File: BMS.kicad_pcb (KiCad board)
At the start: 2 copper layers, 20 x 100 mm, 74 parts, among them Q2 PSMN3R7-100BSE, Q3 PSMN020-100YS, U1 MP2790DFP-0000-T

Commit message: bms layout progress
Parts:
- C_3V1, C_PACK_FLT1, C_REG1, C_REGIN1, C_TOP_FLT1, C_VDD1, D7, U1: moved to B.Cu
- D1, D2, D3, D4, D5, D6, D_CHG_VGS1, D_CHG_VGS2, MBAL_1, MBAL_2, MBAL_3, MBAL_4, MBAL_5, MBAL_6, R_BAL_5, R_BAL_6, R_CHG_PUP1, R_DSG_PUP1, R_GATE6: moved to F.Cu
- moved C_CELL_FLT6 82.0 mm to (210.1, 118.6), turned to 180 degrees
- moved MBAL_6 81.1 mm to (210.1, 113.2), turned to 90 degrees
- moved D_CHG_VGS2 81.0 mm to (208.8, 41.0), turned to -90 degrees
- moved R_CELL_FLT4 78.5 mm to (210.1, 117.0), turned to 180 degrees
- moved C_SRP_GND1 77.5 mm to (117.2, 101.9), turned to 90 degrees
- moved Q2 77.0 mm to (209.8, 53.6), turned to -90 degrees
- moved C_PACK_E1 76.6 mm to (106.0, 96.4)
- moved C_CELL_FLT5 74.8 mm to (210.1, 107.3), turned to 180 degrees
- moved C_SRN_GND1 74.7 mm to (114.7, 101.9), turned to 90 degrees
- moved C_SRN_SRP1 73.4 mm to (119.6, 101.9), turned to -90 degrees
- moved MBAL_5 71.2 mm to (209.9, 105.0), turned to 90 degrees
- moved C_CELL_FLT4 70.3 mm to (209.9, 99.3)
- moved D_CHG_VGS1 66.8 mm to (212.5, 63.4), turned to 90 degrees
- moved C_CELL_FLT3 66.2 mm to (209.9, 91.3), turned to 180 degrees
- moved D7 65.5 mm to (107.3, 85.3), turned to -90 degrees
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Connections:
- Q2 pad 3: /main/BMS/TOP -> /main/BMS/BATT+
- Q3 pad 3: /main/BMS/BATT+ -> /main/BMS/TOP
- R_CHG_MG1 pad 2: Net-(Q2-G) -> Net-(Q3-G)
- R_DSG_MG1 pad 2: Net-(Q3-G) -> Net-(Q2-G)
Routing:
- net /main/BMS/TOP: track 0.00 -> 1.62 mm
- added copper zone on B.Cu, net Net-(U1-VMID)
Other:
- copper layers 2 -> 4

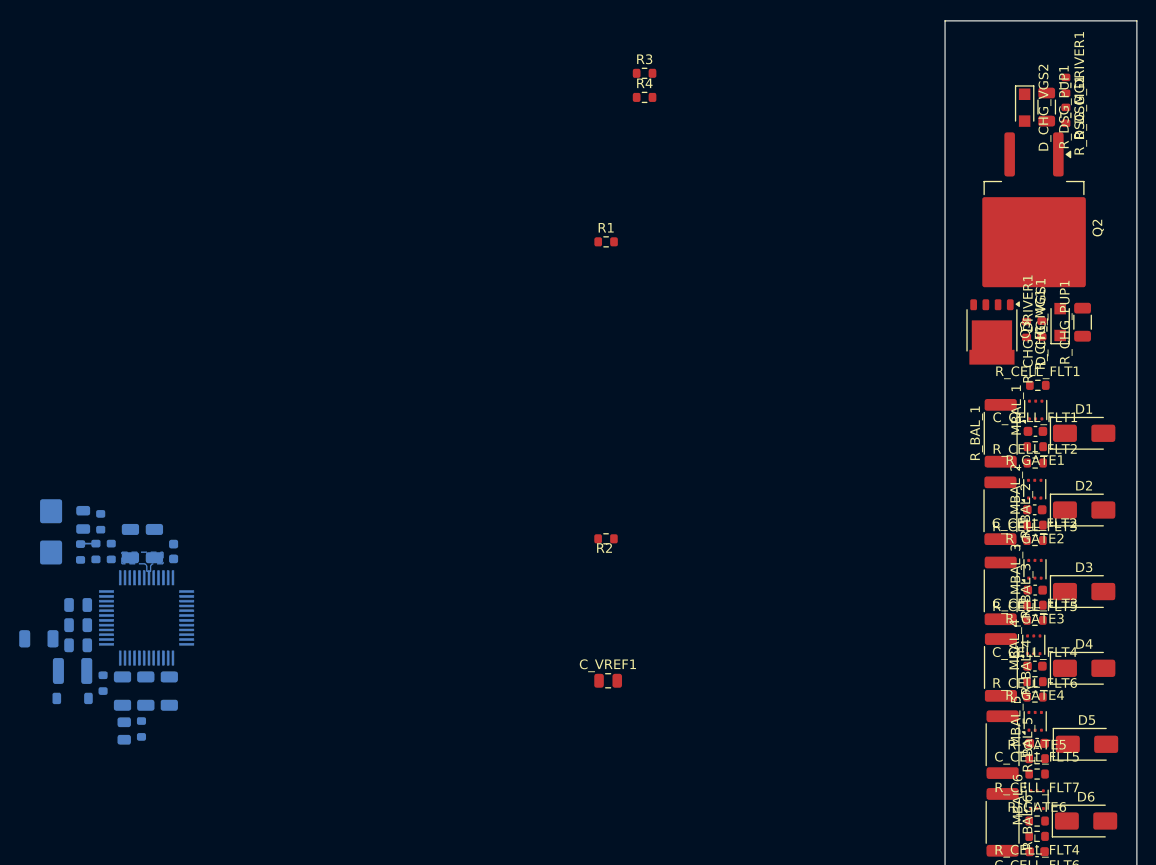
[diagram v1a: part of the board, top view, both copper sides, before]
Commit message: Updating schematic and adding in compnents to the PCB
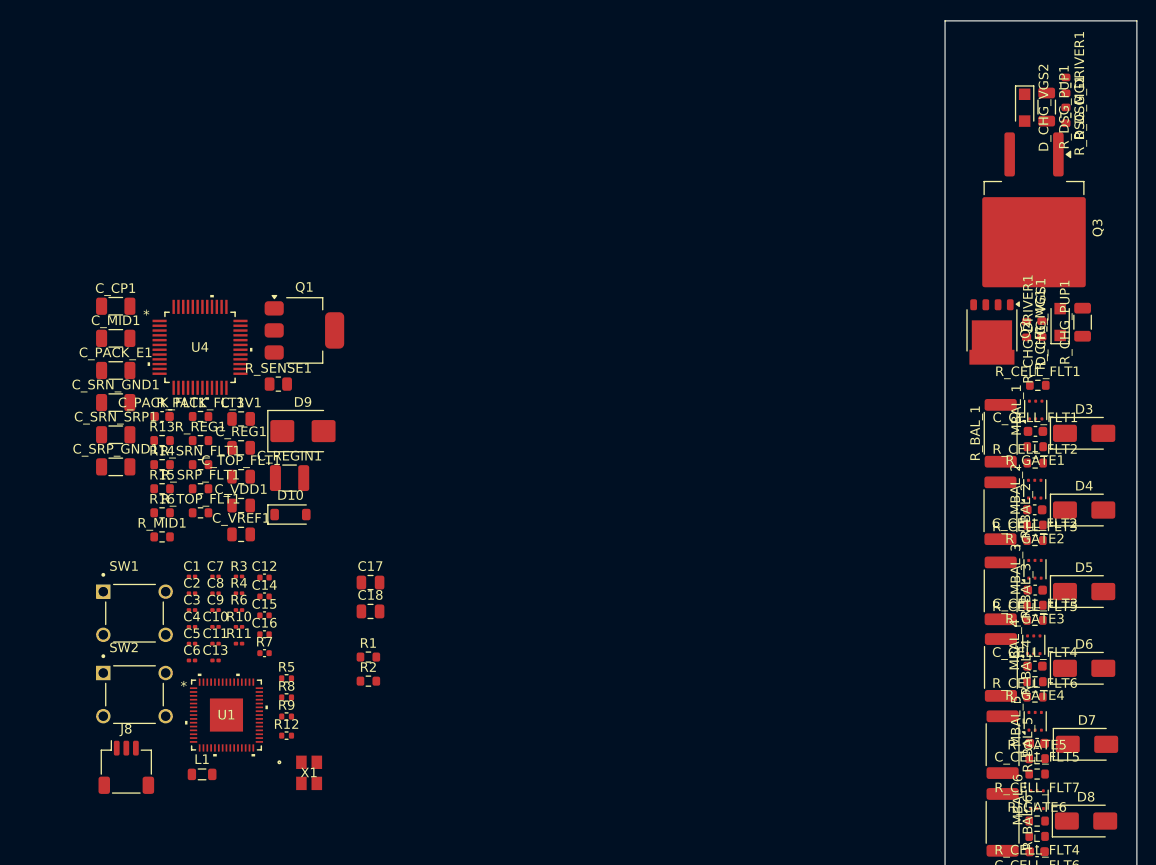
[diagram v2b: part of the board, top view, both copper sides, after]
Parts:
- removed the D7 at (107.3, 85.3)
- removed the D8 at (109.5, 102.6)
- added C1: 100n, Capacitor_SMD:C_0201_0603Metric, F.Cu at (122.0, 89.9)
- added C10: 100n, Capacitor_SMD:C_0201_0603Metric, F.Cu at (124.4, 95.2)
- added C11: 100n, Capacitor_SMD:C_0201_0603Metric, F.Cu at (124.4, 96.9)
- added C12: 4.7u, Capacitor_SMD:C_0402_1005Metric, F.Cu at (129.6, 90.0)
- added C13: 100n, Capacitor_SMD:C_0201_0603Metric, F.Cu at (124.4, 98.7)
- added C14: 4.7u, Capacitor_SMD:C_0402_1005Metric, F.Cu at (129.6, 92.0)
- added C15: 4.7u, Capacitor_SMD:C_0402_1005Metric, F.Cu at (129.6, 94.0)
- added C16: 4.7u, Capacitor_SMD:C_0402_1005Metric, F.Cu at (129.6, 96.0)
- added C17: 10uF, Capacitor_SMD:C_0805_2012Metric, F.Cu at (140.6, 90.6)
- added C18: 10uF, Capacitor_SMD:C_0805_2012Metric, F.Cu at (140.6, 93.6)
- added C2: 100n, Capacitor_SMD:C_0201_0603Metric, F.Cu at (122.0, 91.7)
- added C3: 100n, Capacitor_SMD:C_0201_0603Metric, F.Cu at (122.0, 93.4)
- added C4: 100n, Capacitor_SMD:C_0201_0603Metric, F.Cu at (122.0, 95.2)
- added C5: 100n, Capacitor_SMD:C_0201_0603Metric, F.Cu at (122.0, 96.9)
- added C6: 100n, Capacitor_SMD:C_0201_0603Metric, F.Cu at (122.0, 98.7)
- added C7: 15p, Resistor_SMD:R_0201_0603Metric, F.Cu at (124.4, 89.9)
- added C8: 15p, Resistor_SMD:R_0201_0603Metric, F.Cu at (124.4, 91.7)
- added C9: 100n, Capacitor_SMD:C_0201_0603Metric, F.Cu at (124.4, 93.4)
- added D10: BAT46GWJ, Diode_SMD:D_SOD-123, F.Cu at (132.3, 83.5)
- added D9: TPSMB28CA-VR, Diode_SMD:D_SMB, F.Cu at (133.6, 74.8)
- added J8: Conn_01x03_Pin, Connector_JST:JST_SH_SM03B-SRSS-TB_1x03-1MP_P1.00mm_Horizontal, F.Cu at (115.1, 109.8)
- added L1: 3.3u, Inductor_SMD:L_0805_2012Metric, F.Cu at (123.0, 110.6)
- added Q1: FZT853TA, Package_TO_SOT_SMD:SOT-223-3_TabPin2, F.Cu at (133.7, 64.3)
- added R10: 27, Resistor_SMD:R_0201_0603Metric, F.Cu at (126.9, 95.2)
- added R11: 27, Resistor_SMD:R_0201_0603Metric, F.Cu at (126.9, 96.9)
- added R12: 33, Resistor_SMD:R_0402_1005Metric, F.Cu at (131.9, 106.5)
- added R13: 10k, Resistor_SMD:R_0603_1608Metric, F.Cu at (118.9, 75.8)
- added R14: 10k, Resistor_SMD:R_0603_1608Metric, F.Cu at (118.9, 78.3)
- added R15: 10k, Resistor_SMD:R_0603_1608Metric, F.Cu at (118.9, 80.8)
- added R16: 10k, Resistor_SMD:R_0603_1608Metric, F.Cu at (118.9, 83.3)
- added R5: 1k, Resistor_SMD:R_0402_1005Metric, F.Cu at (131.9, 100.6)
- added R6: 1k, Resistor_SMD:R_0201_0603Metric, F.Cu at (126.9, 93.4)
- added R7: 100, Capacitor_SMD:C_0402_1005Metric, F.Cu at (129.6, 97.9)
- added R8: 1, Resistor_SMD:R_0402_1005Metric, F.Cu at (131.9, 102.5)
- added R9: 1k, Resistor_SMD:R_0402_1005Metric, F.Cu at (131.9, 104.5)
- added SW1: SW_Push, _BMS:SW_TS02-66-43-BK-160-LCR-D, F.Cu at (116.0, 93.8)
- added SW2: SW_Push, _BMS:SW_TS02-66-43-BK-160-LCR-D, F.Cu at (116.0, 102.2)
- added U4: MP2790DFP-0000-T, _BMS:TQFP-48_MP2790_MNP, F.Cu at (122.8, 66.0)
- added X1: ABM8-272-T3, _BMS:ABM8-272-T3_ABR, F.Cu at (134.2, 110.4)
- C_3V1, C_CP1, C_MID1, C_PACK_E1, C_PACK_FLT1, C_REG1, C_REGIN1, C_SRN_GND1, C_SRN_SRP1, C_SRP_GND1, C_TOP_FLT1, C_VDD1, R_MID1, R_PACK_FLT1, R_REG1, R_SENSE1, R_SRN_FLT1, R_SRP_FLT1, R_TOP_FLT1: moved to F.Cu
- R1, R2: value 10k -> 5.1k
- R3, R4: value 10k -> 100; footprint Resistor_SMD:R_0603_1608Metric -> Resistor_SMD:R_0201_0603Metric
- U1: value MP2790DFP-0000-T -> RP2350A; footprint _BMS:QFP50P900X900X120-48N -> _BMS:QFN-60_7X7_RPI; moved to F.Cu
- moved R3 67.4 mm to (126.9, 89.9)
- moved R4 66.8 mm to (126.9, 91.7)
- moved R1 49.9 mm to (140.4, 98.3)
- moved C_VREF1 41.2 mm to (127.1, 85.5)
- moved R_SENSE1 39.6 mm to (131.0, 69.9), turned to 0 degrees
- moved C_REGIN1 30.3 mm to (132.2, 79.7)
- moved C_SRN_GND1 30.1 mm to (114.0, 71.8), turned to 0 degrees
- moved C_PACK_E1 29.1 mm to (114.0, 68.5)
- moved C_3V1 29.1 mm to (127.1, 73.5)
- moved R2 28.9 mm to (140.4, 100.8)
- moved C_SRN_SRP1 27.3 mm to (114.0, 75.2), turned to 0 degrees
- moved R_SRP_FLT1 25.8 mm to (122.9, 80.8), turned to 0 degrees
- moved R_SRN_FLT1 24.9 mm to (122.9, 78.3), turned to 0 degrees
- moved C_CP1 24.8 mm to (114.0, 61.8), turned to 0 degrees
- moved C_SRP_GND1 23.6 mm to (114.0, 78.5), turned to 0 degrees
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- renumbered D1 to D3, D2 to D4, D3 to D5, D4 to D6, D5 to D7, D6 to D8, Q3 to Q2, Q2 to Q3
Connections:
- C_3V1 pad 2: Net-(U1-3V3) -> Net-(U4-3V3)
- C_CP1 pad 2: Net-(U1-VMID) -> Net-(U4-VMID)
- C_MID1 pad 1: Net-(U1-VMID) -> Net-(U4-VMID)
- C_PACK_FLT1 pad 2: Net-(U1-PACKP) -> Net-(U4-PACKP)
- C_REGIN1 pad 2: /main/BMS/REGIN -> /main/INT_5V
- C_TOP_FLT1 pad 1: Net-(U1-VTOP) -> Net-(U4-VTOP)
- C_VDD1 pad 1: Net-(U1-VDD) -> Net-(U4-VDD)
- C_VREF1 pad 2: Net-(U1-VREF) -> Net-(U4-VREF)
- R1 pad 1: /main/BMS/NTC4 -> GND
- R1 pad 2: /main/BMS/AGND -> Net-(J1-CC1_A)
- R2 pad 1: /main/BMS/NTC3 -> GND
- R2 pad 2: /main/BMS/AGND -> Net-(J1-CC1_B)
- R3 pad 1: /main/BMS/NTC2 -> Net-(J8-Pin_1)
- R3 pad 2: /main/BMS/AGND -> /main/microcontroller/SWCLK
- R4 pad 1: /main/BMS/NTC1 -> /main/microcontroller/SWDIO
- R4 pad 2: /main/BMS/AGND -> Net-(J8-Pin_3)
- R_MID1 pad 1: Net-(U1-VMID) -> Net-(U4-VMID)
- R_PACK_FLT1 pad 1: Net-(U1-PACKP) -> Net-(U4-PACKP)
- R_TOP_FLT1 pad 2: Net-(U1-VTOP) -> Net-(U4-VTOP)
- U1 pad 1: /main/BMS/CELL_6 -> +3V3
- U1 pad 10: /main/BMS/CELL_4 -> unconnected-(U1-GPIO7-Pad10)
- U1 pad 11: /main/BMS/CELL_3 -> +3V3
- U1 pad 12: /main/BMS/CELL_2 -> unconnected-(U1-GPIO8-Pad12)
- U1 pad 13: /main/BMS/CELL_1 -> unconnected-(U1-GPIO9-Pad13)
- U1 pad 14: /main/BMS/CELL_0 -> /main/BMS/XALERT
- U1 pad 15: /main/BMS/SRP -> /main/BMS/NSHDN
- U1 pad 16: /main/BMS/SRN -> /main/BMS/WDT
- U1 pad 17: /main/BMS/NTC4 -> unconnected-(U1-GPIO13-Pad17)
- U1 pad 18: /main/BMS/NTC3 -> unconnected-(U1-GPIO14-Pad18)
- U1 pad 19: /main/BMS/NTC2 -> unconnected-(U1-GPIO15-Pad19)
- U1 pad 2: /main/BMS/CELL_6 -> /main/BMS/SDA
- U1 pad 20: /main/BMS/NTC1 -> +3V3
- U1 pad 21: /main/BMS/AGND -> /main/microcontroller/XIN
- U1 pad 22: Net-(U1-VREF) -> /main/microcontroller/XOUT
- U1 pad 23: /main/BMS/AGND -> +1V1
- U1 pad 24: Net-(Q1-B) -> /main/microcontroller/SWCLK
- U1 pad 25: /main/BMS/REGIN -> /main/microcontroller/SWDIO
- U1 pad 26: Net-(U1-3V3) -> Net-(U1-RUN)
- U1 pad 27: Net-(U1-VDD) -> unconnected-(U1-GPIO16-Pad27)
- U1 pad 3: /main/BMS/CELL_6 -> /main/BMS/SCL
- U1 pad 30: unconnected-(U1-NSHDN-Pad30) -> +3V3
- U1 pad 31: /main/BMS/SCL -> unconnected-(U1-GPIO19-Pad31)
- U1 pad 32: /main/BMS/SDA -> unconnected-(U1-GPIO20-Pad32)
- U1 pad 38: Net-(U1-PACKP) -> +3V3
- U1 pad 39: /main/BMS/DSG -> +1V1
- U1 pad 4: /main/BMS/CELL_6 -> unconnected-(U1-GPIO2-Pad4)
- U1 pad 42: /main/BMS/VCP -> unconnected-(U1-GPIO28_ADC2-Pad42)
- U1 pad 43: Net-(U1-VMID) -> unconnected-(U1-GPIO29_ADC3-Pad43)
- U1 pad 44: /main/BMS/CHG -> /main/microcontroller/ADC_VREF
- U1 pad 45: Net-(U1-VTOP) -> +3V3
- U1 pad 46: /main/BMS/C10 -> Net-(U1-VREG_AVDD)
- U1 pad 47: /main/BMS/C10 -> GND
- U1 pad 48: /main/BMS/C10 -> Net-(U1-VREG_LX)
- U1 pad 5: /main/BMS/CELL_6 -> unconnected-(U1-GPIO3-Pad5)
- U1 pad 6: /main/BMS/CELL_6 -> +1V1
- U1 pad 7: /main/BMS/CELL_6 -> unconnected-(U1-GPIO4-Pad7)
- U1 pad 8: /main/BMS/CELL_6 -> unconnected-(U1-GPIO5-Pad8)
- U1 pad 9: /main/BMS/CELL_5 -> unconnected-(U1-GPIO6-Pad9)
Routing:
- net /main/BMS/TOP: track 1.62 -> 0.00 mm
- removed copper zone on B.Cu, net Net-(U1-VMID)

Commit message: schematic progress
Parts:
- C1, C10, C11, C12, C13, C14, C15, C16, C2, C3, C4, C5, C6, C7, C8, C9, C_3V1, C_CP1, C_MID1, C_PACK_FLT1, C_REG1, C_REGIN1, C_SRN_GND1, C_SRN_SRP1, C_SRP_GND1, C_TOP_FLT1, C_VDD1, C_VREF1, J8, L1, Q1, R10, R11, R12, R13, R14, R15, R16, R3, R4, R6, R7, R8, R_MID1, R_PACK_FLT1, R_REG1, R_SRN_FLT1, R_SRP_FLT1, R_TOP_FLT1, U1, U4, X1: moved to B.Cu
- moved J8 121.5 mm to (226.8, 61.9), turned to -90 degrees
- moved C_SRP_GND1 108.6 mm to (221.4, 95.3), turned to -90 degrees
- moved C_MID1 108.4 mm to (221.9, 75.0)
- moved C_SRN_GND1 107.6 mm to (219.0, 95.3), turned to 90 degrees
- moved C_SRN_SRP1 107.4 mm to (220.2, 91.7)
- moved R13 106.3 mm to (224.3, 89.4)
- moved R14 106.2 mm to (224.3, 91.0)
- moved R15 106.0 mm to (224.3, 92.5)
- moved R16 106.0 mm to (224.3, 94.0)
- moved L1 105.8 mm to (215.2, 58.6)
- moved C_CP1 105.5 mm to (218.4, 77.4), turned to 90 degrees
- moved C1 102.9 mm to (221.3, 63.0), turned to 180 degrees
- moved C2 102.9 mm to (221.3, 65.0), turned to 180 degrees
- moved C3 102.8 mm to (221.3, 67.0), turned to 180 degrees
- moved R_SRP_FLT1 101.7 mm to (223.4, 96.3), turned to 90 degrees
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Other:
- board size 20 x 100 mm -> 30 x 70 mm

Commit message: Layed on board. Still need to route
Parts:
- removed C17: 10uF, Capacitor_SMD:C_0805_2012Metric
- removed the C4 at (217.6, 70.7)
- removed MBAL_1, MBAL_2, MBAL_3, MBAL_4, MBAL_5, MBAL_6: MOSFET, _BMS:SC70-6
- added C19: 10n, Capacitor_SMD:C_0402_1005Metric, B.Cu at (145.0, 97.8)
- added C20: 10n, Capacitor_SMD:C_0402_1005Metric, B.Cu at (145.0, 94.5)
- added C21: 10n, Capacitor_SMD:C_0402_1005Metric, B.Cu at (145.0, 92.3)
- added C22: 10uF, Capacitor_SMD:C_0805_2012Metric, B.Cu at (174.5, 72.1)
- added C23: 10uF, Capacitor_SMD:C_0805_2012Metric, B.Cu at (174.4, 81.0)
- added DAGND_CO1: 4.7V 200MW, Diode_SMD:D_SOD-323, F.Cu at (154.4, 82.7)
- added H1: MountingHole, MountingHole:MountingHole_2.2mm_M2_Pad_TopBottom, F.Cu at (149.9, 66.4)
- added H2: MountingHole, MountingHole:MountingHole_2.2mm_M2_Pad_TopBottom, F.Cu at (146.9, 131.4)
- added J1: 12402012E212A, _BMS:AMPHENOL_12402012E212A, B.Cu at (168.4, 107.6)
- added J3: Conn_01x02_Socket, Connector_AMASS:AMASS_XT30PW-F_1x02_P2.50mm_Horizontal, F.Cu at (150.1, 78.9)
- added J5: Conn_01x10_Pin, _BMS:TB4-Hirose, F.Cu at (158.9, 98.9)
- added J6: Conn_01x02_Pin, Connector_AMASS:AMASS_XT30PW-M_1x02_P2.50mm_Horizontal, F.Cu at (150.9, 124.4)
- added NT1: NetTie_2, NetTie:NetTie-3_SMD_Pad0.5mm, F.Cu at (181.2, 89.1)
- added Q4: PSMN3R7-100BSE, _BMS:TO-263-2, F.Cu at (138.8, 105.4)
- added Q5: PSMN3R7-100BSE, _BMS:TO-263-2, F.Cu at (138.8, 91.4)
- added R_CHG_MG2: 100 Ω, Resistor_SMD:R_0402_1005Metric, B.Cu at (144.4, 120.5)
- added R_DSG_MG2: 100 Ω, Resistor_SMD:R_0402_1005Metric, B.Cu at (131.4, 105.4)
- added U1: USBLC6-2SC6, Package_TO_SOT_SMD:SOT-23-6, B.Cu at (160.4, 107.4)
- added U10: SQ1464EEH-T1_GE3, _BMS:SC70-6, F.Cu at (150.9, 85.9)
- added U12: TPS7B8133QDGNRQ1, _BMS:VSSOP8_DGN_TEX, B.Cu at (174.4, 76.5)
- added U2: USBLC6-2SC6, Package_TO_SOT_SMD:SOT-23-6, F.Cu at (192.1, 85.5)
- added U5: SQ1464EEH-T1_GE3, _BMS:SC70-6, F.Cu at (150.9, 110.9)
- added U6: SQ1464EEH-T1_GE3, _BMS:SC70-6, F.Cu at (150.9, 105.9)
- added U7: SQ1464EEH-T1_GE3, _BMS:SC70-6, F.Cu at (150.9, 100.8)
- added U8: SQ1464EEH-T1_GE3, _BMS:SC70-6, F.Cu at (150.9, 95.9)
- added U9: SQ1464EEH-T1_GE3, _BMS:SC70-6, F.Cu at (150.9, 90.9)
- C18: value 10uF -> 10n; footprint Capacitor_SMD:C_0805_2012Metric -> Capacitor_SMD:C_0402_1005Metric; moved to B.Cu
- C_3V1, C_REG1, C_VDD1, C_VREF1: footprint Capacitor_SMD:C_0805_2012Metric -> Capacitor_SMD:C_0402_1005Metric
- C_CELL_FLT1, C_CELL_FLT2, C_CELL_FLT3, C_CELL_FLT4, C_CELL_FLT5, C_CELL_FLT6, C_PACK_FLT1: value 10 nF -> 10n; footprint Capacitor_SMD:C_0603_1608Metric -> Capacitor_SMD:C_0402_1005Metric
- C_REGIN1: footprint Capacitor_SMD:C_1210_3225Metric -> Capacitor_SMD:C_0603_1608Metric
- C_TOP_FLT1: footprint Capacitor_SMD:C_0805_2012Metric -> Capacitor_SMD:C_0603_1608Metric
- D3, D4, D5, D6, D7, D8: value D_Zener -> PTVS5V0S1UR,115; footprint Diode_SMD:D_SMA -> Diode_SMD:Nexperia_CFP3_SOD-123W
- D_CHG_VGS1, D_CHG_VGS2, R1, R2: moved to B.Cu
- Q2: footprint Package_TO_SOT_SMD:LFPAK56 -> _BMS:LFPAK56_1
- Q3: value PSMN3R7-100BSE -> PSMN020-100YS; footprint Package_TO_SOT_SMD:TO-263-2 -> _BMS:LFPAK56_1
- R13, R14, R15, R16, R_CELL_FLT1, R_CELL_FLT2, R_CELL_FLT3, R_CELL_FLT4, R_CELL_FLT5, R_CELL_FLT6, R_CELL_FLT7, R_GATE1, R_GATE2, R_GATE3, R_GATE4, R_GATE5, R_GATE6, R_PACK_FLT1, R_REG1, R_SRN_FLT1, R_SRP_FLT1, R_TOP_FLT1: footprint Resistor_SMD:R_0603_1608Metric -> Resistor_SMD:R_0402_1005Metric
- R_BAL_1, R_BAL_2, R_BAL_3, R_BAL_4, R_BAL_5, R_BAL_6: footprint Resistor_SMD:R_2512_6332Metric -> Resistor_SMD:R_1206_3216Metric
- R_CHG_DRIVER1, R_CHG_MG1, R_DSG_DRIVER1, R_DSG_MG1: footprint Resistor_SMD:R_0603_1608Metric -> Resistor_SMD:R_0402_1005Metric; moved to B.Cu
- R_CHG_PUP1, R_DSG_PUP1: footprint Resistor_SMD:R_1206_3216Metric -> Resistor_SMD:R_0402_1005Metric; moved to B.Cu
- R_SENSE1: footprint Resistor_SMD:R_0805_2012Metric -> Resistor_SMD:R_2512_6332Metric
- moved Q2 108.3 mm to (139.2, 116.5)
- moved D_CHG_VGS1 101.1 mm to (144.4, 117.5), turned to -90 degrees
- moved Q3 101.0 mm to (139.2, 122.5), turned to 180 degrees
- moved R_CHG_MG1 100.8 mm to (144.4, 114.5), turned to 0 degrees
- moved R_DSG_PUP1 100.3 mm to (131.4, 98.4), turned to 0 degrees
- moved R_CHG_PUP1 98.2 mm to (146.2, 117.5), turned to -90 degrees
- moved R_DSG_MG1 97.5 mm to (131.4, 91.4), turned to 0 degrees
- moved D_CHG_VGS2 95.7 mm to (134.9, 98.4), turned to 180 degrees
- moved D4 87.5 mm to (147.4, 106.9), turned to -90 degrees
- moved R_DSG_DRIVER1 86.0 mm to (149.1, 92.7), turned to 90 degrees
- moved R_GATE2 82.2 mm to (149.4, 108.4), turned to 90 degrees
- moved C_CELL_FLT2 81.6 mm to (150.9, 108.4), turned to 90 degrees
- moved R_CHG_DRIVER1 80.2 mm to (153.1, 92.7), turned to 90 degrees
- moved R_CELL_FLT1 79.9 mm to (147.4, 115.0)
- moved R13 79.8 mm to (145.0, 98.9), turned to 180 degrees
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- renumbered C11 to C10, C12 to C11, C13 to C12, C14 to C13, C15 to C14, C16 to C15, C5 to C4, C6 to C5, C7 to C6, C8 to C7, C9 to C8, C10 to C9, J8 to J4, U4 to U11, U1 to U3
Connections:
- C18 pad 1: +3V3 -> GNDREF
- C18 pad 2: GND -> /main/BMS/NTC4
- C_3V1 pad 1: /main/BMS/AGND -> Net-(U11-3V3)
- C_3V1 pad 2: Net-(U4-3V3) -> GNDREF
- C_MID1 pad 2: /main/BMS/AGND -> GNDREF
- C_PACK_E1 pad 1: /main/BMS/BATT+ -> /main/BMS/PACK+
- C_PACK_E1 pad 2: /main/BMS/PGNDE -> GND
- C_PACK_FLT1 pad 1: /main/BMS/AGND -> Net-(U11-PACKP)
- C_PACK_FLT1 pad 2: Net-(U4-PACKP) -> GNDREF
- C_REG1 pad 2: /main/BMS/AGND -> GNDREF
- C_REGIN1 pad 1: /main/BMS/AGND -> GNDREF
- C_SRN_GND1 pad 1: /main/BMS/AGND -> GNDREF
- C_SRP_GND1 pad 2: /main/BMS/AGND -> GNDREF
- C_TOP_FLT1 pad 2: /main/BMS/AGND -> GNDREF
- C_VDD1 pad 2: /main/BMS/AGND -> GNDREF
- C_VREF1 pad 1: /main/BMS/AGND -> GNDREF
- D10 pad 1: /main/BMS/BATT+ -> /main/BMS/PACK+
- D10 pad 2: /main/BMS/PGNDE -> GND
- D_CHG_VGS2 pad 2: /main/BMS/BATT+ -> /main/BMS/PACK+
- Q3 pad 3: /main/BMS/BATT+ -> /main/BMS/TOP
- R11 pad 2: /main/external_io/D+ -> /main/external_io/D-
- R13 pad 2: /main/BMS/AGND -> GNDREF
- R14 pad 2: /main/BMS/AGND -> GNDREF
- R15 pad 2: /main/BMS/AGND -> GNDREF
- R16 pad 2: /main/BMS/AGND -> GNDREF
- R_CELL_FLT4 pad 1: GND -> /main/BMS/C3
- R_CELL_FLT4 pad 2: /main/BMS/CELL_0 -> /main/BMS/CELL_3
- R_CELL_FLT5 pad 1: /main/BMS/C3 -> /main/BMS/C2
- R_CELL_FLT5 pad 2: /main/BMS/CELL_3 -> /main/BMS/CELL_2
- R_CELL_FLT6 pad 1: /main/BMS/C2 -> /main/BMS/C1
- R_CELL_FLT6 pad 2: /main/BMS/CELL_2 -> /main/BMS/CELL_1
- R_CELL_FLT7 pad 1: /main/BMS/C1 -> GND
- R_CELL_FLT7 pad 2: /main/BMS/CELL_1 -> /main/BMS/CELL_0
- R_DSG_MG1 pad 2: Net-(Q3-G) -> Net-(Q5-G)
- R_DSG_PUP1 pad 2: /main/BMS/BATT+ -> /main/BMS/PACK+
- R_PACK_FLT1 pad 1: Net-(U4-PACKP) -> Net-(U11-PACKP)
- R_SENSE1 pad 2: /main/BMS/PGNDE -> /main/BMS/PACK-
- R_SRN_FLT1 pad 2: /main/BMS/PGNDE -> /main/BMS/PACK-
- U11 pad 21: /main/BMS/AGND -> GNDREF
- U11 pad 23: /main/BMS/AGND -> GNDREF
- U11 pad 26: Net-(U4-3V3) -> Net-(U11-3V3)
- U11 pad 38: Net-(U4-PACKP) -> Net-(U11-PACKP)
- U3 pad 20: +3V3 -> unconnected-(U3-IOVDD-Pad20)
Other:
- board size 30 x 70 mm -> 44 x 71 mm
